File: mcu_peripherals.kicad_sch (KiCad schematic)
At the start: 81 parts, among them J2 USB_C_Receptacle_USB2.0_16P, J3 Conn_01x05, J4 Micro_SD_Card_Det_Hirose_DM3AT, SW1 RESET, SW2 BOOT, U12 USBLC6-2SC6, U14 TPS3840DL30DBVR, U15 ATECC608B-SSHDA, U16 USBLC6-2SC6, U17 ASM330LHHTR, U18 TCA9535PWR, U20 W25N01GVZEIG, U23 TPS22918TDBVTQ1, U802 TMP1075DGKR, U902 SN74AXC4T245QPWRQ1, U903 SN74AXC4T245QPWRQ1

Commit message: Update mcu_peripherals.kicad_sch
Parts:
- removed R12: DNP, Resistor_SMD:R_0603_1608Metric, symbol Device:R
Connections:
- net at U14.1 (~{RESET}): now also C53.1, J3.2 (Pin_2), R25.2, SW1.2, TP14.1, U19.3 (Reset/Enable(EN))
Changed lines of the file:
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@@
 	(wire
 		(pts
-			(xy 115.57 87.63) (xy 109.22 87.63)
+			(xy 109.22 87.63) (xy 137.16 87.63)
 		)
 		(stroke
@@
 	(wire
 		(pts
-			(xy 123.19 87.63) (xy 137.16 87.63)
-		)
-		(stroke
-			(width 0)
-			(type default)
-		)
-	)
-	(wire
-		(pts
 			(xy 219.71 102.87) (xy 219.71 128.27)
 		)
@@
 					(unit 1)
 				)
-			)
-		)
-	)
-	(symbol
-		(lib_id "Device:R")
-		(at 119.38 87.63 90)
-		(mirror x)
-		(unit 1)
-		(body_style 1)
-		(exclude_from_sim no)
-		(in_bom yes)
-		(on_board yes)
-		(in_pos_files yes)
-		(dnp yes)
-		(property "Reference" "R12"
-			(at 117.348 84.836 90)
-			(show_name no)
-			(do_not_autoplace no)
-			(effects
-				(font
-					(size 1.27 1.27)
-				)
-				(justify right)
-			)
-		)
-		(property "Value" "DNP"
-			(at 117.602 89.916 90)
-			(show_name no)
-			(do_not_autoplace no)
-			(effects
-				(font
-					(size 1.27 1.27)
-				)
-				(justify right)
-			)
-		)
-		(property "Footprint" "Resistor_SMD:R_0603_1608Metric"
-			(at 119.38 85.852 90)
-			(hide yes)
-			(show_name no)
-			(do_not_autoplace no)
-			(effects
-				(font
-					(size 1.27 1.27)
-				)
-			)
-		)
-		(property "Datasheet" ""
-			(at 119.38 87.63 0)
-			(hide yes)
-			(show_name no)
-			(do_not_autoplace no)
-			(effects
-				(font
-					(size 1.27 1.27)
-				)
-			)
-		)
-		(property "Description" "Resistor"
-			(at 119.38 87.63 0)
-			(hide yes)
-			(show_name no)
-			(do_not_autoplace no)
-			(effects
-				(font
-					(size 1.27 1.27)
-				)
-			)
-		)
-		(pin "1"
-		)
-		(pin "2"
-		)
-		(instances
-			(project "Tracker"
-				(path "/586d1ea1-b017-4713-987c-545d658f6cc8/378094db-8f3e-4510-9f4d-07bbb8577682"
-					(reference "R12")
-					(unit 1)
-				)
-			)
-			(project "page_2"
-				(path "/b70b23fc-d90a-4374-8ce9-83c1fd111d3f"
-					(reference "R215")
-					(unit 1)
-				)

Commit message: update
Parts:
- renumbered C44 to C51, C48 to C52, C49 to C53, C50 to C54, C51 to C55, C52 to C56, C53 to C57, C54 to C58, C55 to C59, C56 to C60, C58 to C61, C57 to C62, C59 to C63, C60 to C64, C64 to C65, C65 to C66, C66 to C67, C67 to C68, C68 to C69, C69 to C70, D1 to D3, J2 to J3, J3 to J4, J4 to J5, R601 to R43, R602 to R44, R202 to R45, R204 to R46, R203 to R47, R201 to R48, R25 to R49, R20 to R50, R22 to R51, R24 to R52, R38 to R53, R34 to R54, R30 to R55, R906 to R56, R209 to R57, R205 to R58, R41 to R59, R48 to R60, R51 to R61, R53 to R62, R55 to R63, R54 to R64, R56 to R65, R904 to R66, R57 to R67, R905 to R68, R58 to R69, TP2 to TP15, TP205 to TP16, TP204 to TP17, TP14 to TP18, TP211 to TP19, TP210 to TP20, TP201 to TP21, TP403 to TP22, TP12 to TP23, TP13 to TP24, TP15 to TP25, TP16 to TP26, TP17 to TP27, U14 to U13, U12 to U14, U802 to U15, U15 to U16, U16 to U17, U17 to U18, U18 to U19, U19 to U20, U20 to U21, U903 to U22, U902 to U23, U23 to U24

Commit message: udt
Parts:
- renumbered SW2 to BOOT, SW1 to RESET
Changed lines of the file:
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@@
 		(dnp no)
 		(fields_autoplaced yes)
-		(property "Reference" "SW2"
+		(property "Reference" "BOOT"
 			(at 440.69 139.6999 90)
 			(show_name no)
@@
 			(project "Tracker"
 				(path "/586d1ea1-b017-4713-987c-545d658f6cc8/378094db-8f3e-4510-9f4d-07bbb8577682"
-					(reference "SW2")
+					(reference "BOOT")
 					(unit 1)
 				)
@@
 		(dnp no)
 		(fields_autoplaced yes)
-		(property "Reference" "SW1"
+		(property "Reference" "RESET"
 			(at 135.89 91.4399 90)
 			(show_name no)
@@
 			(project "Tracker"
 				(path "/586d1ea1-b017-4713-987c-545d658f6cc8/378094db-8f3e-4510-9f4d-07bbb8577682"
-					(reference "SW1")
+					(reference "RESET")
 					(unit 1)
 				)

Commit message: BT1 update
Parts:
- renumbered BOOT to BOOT1, RESET to RESET1
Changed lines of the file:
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@@
 		(dnp no)
 		(fields_autoplaced yes)
-		(property "Reference" "BOOT"
+		(property "Reference" "BOOT1"
 			(at 440.69 139.6999 90)
 			(show_name no)
@@
 			(project "Tracker"
 				(path "/586d1ea1-b017-4713-987c-545d658f6cc8/378094db-8f3e-4510-9f4d-07bbb8577682"
-					(reference "BOOT")
+					(reference "BOOT1")
 					(unit 1)
 				)
@@
 		(dnp no)
 		(fields_autoplaced yes)
-		(property "Reference" "RESET"
+		(property "Reference" "RESET1"
 			(at 135.89 91.4399 90)
 			(show_name no)
@@
 			(project "Tracker"
 				(path "/586d1ea1-b017-4713-987c-545d658f6cc8/378094db-8f3e-4510-9f4d-07bbb8577682"
-					(reference "RESET")
+					(reference "RESET1")
 					(unit 1)
 				)

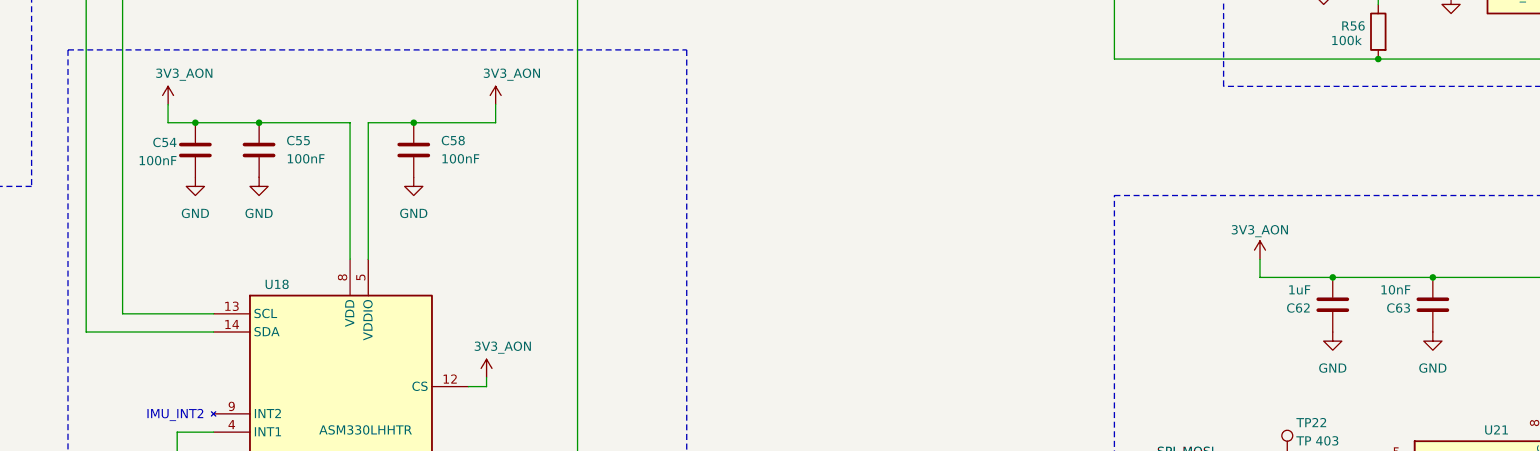
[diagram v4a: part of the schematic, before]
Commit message: relocation of TP
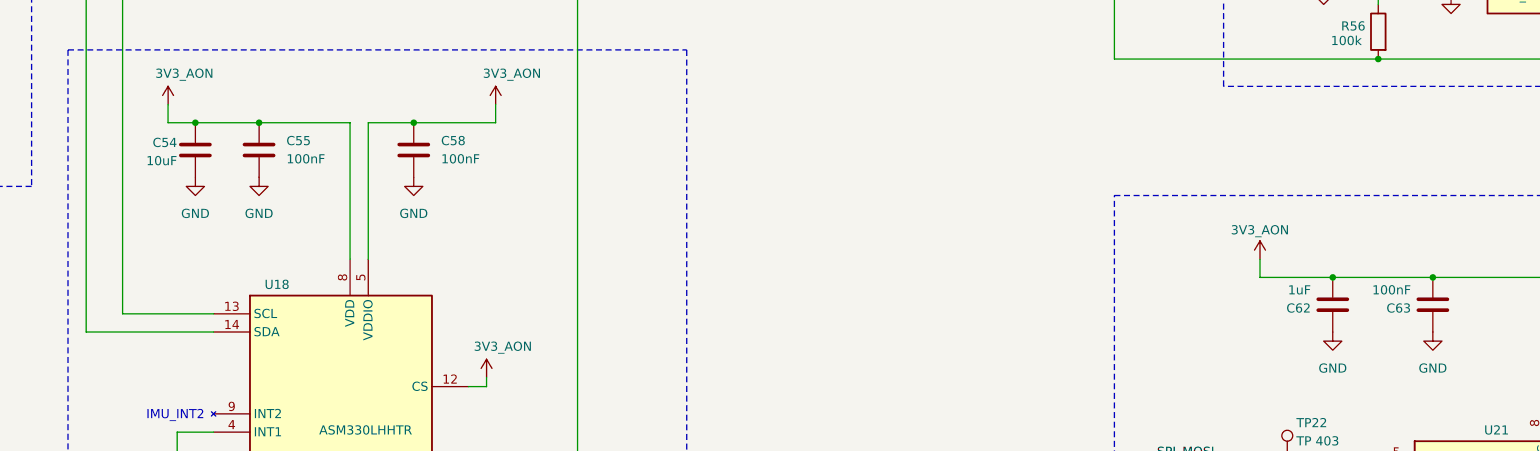
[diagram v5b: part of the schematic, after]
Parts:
- C54: value 100nF -> 10uF
- C63: value 10nF -> 100nF
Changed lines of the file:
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@@
 			)
 		)
-		(property "Value" "10nF"
+		(property "Value" "100nF"
 			(at 341.122 331.978 0)
 			(show_name no)
@@
 			)
 		)
-		(property "Value" "100nF"
+		(property "Value" "10uF"
 			(at 168.91 313.944 0)
 			(show_name no)
